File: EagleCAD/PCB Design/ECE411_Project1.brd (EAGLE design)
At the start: 160 x 100 mm, 38 parts, among them J1 0473460001_USBMICRO, U1 ATS160SM-1, U2 MIC29310-5.0WU, U3 NCP5501DT50RKG, U4 DCJACK_2.1MM_PTH

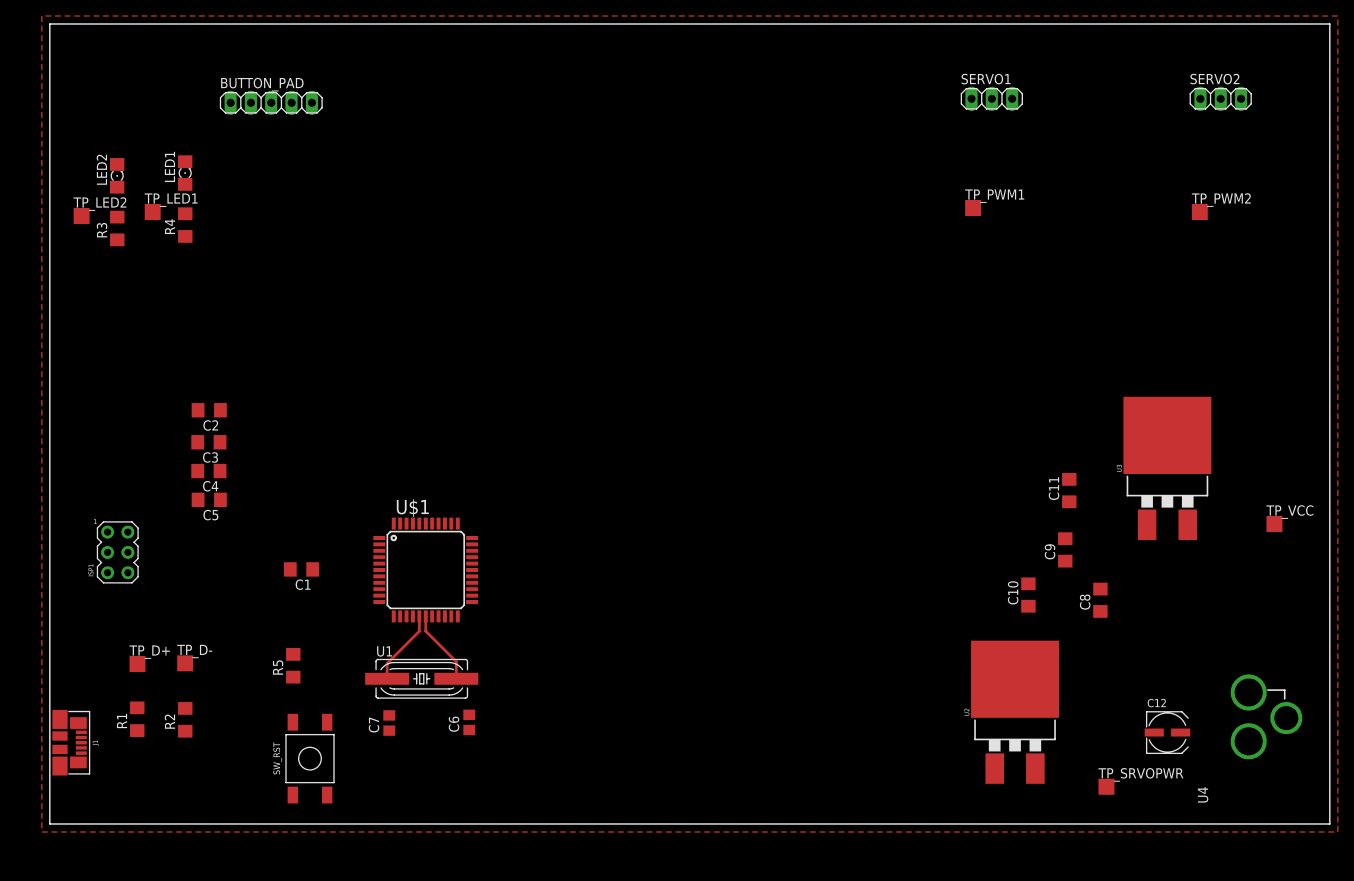
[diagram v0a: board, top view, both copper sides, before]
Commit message: in-progress updates: Connected Vbuses in schematic, organized the new layout design
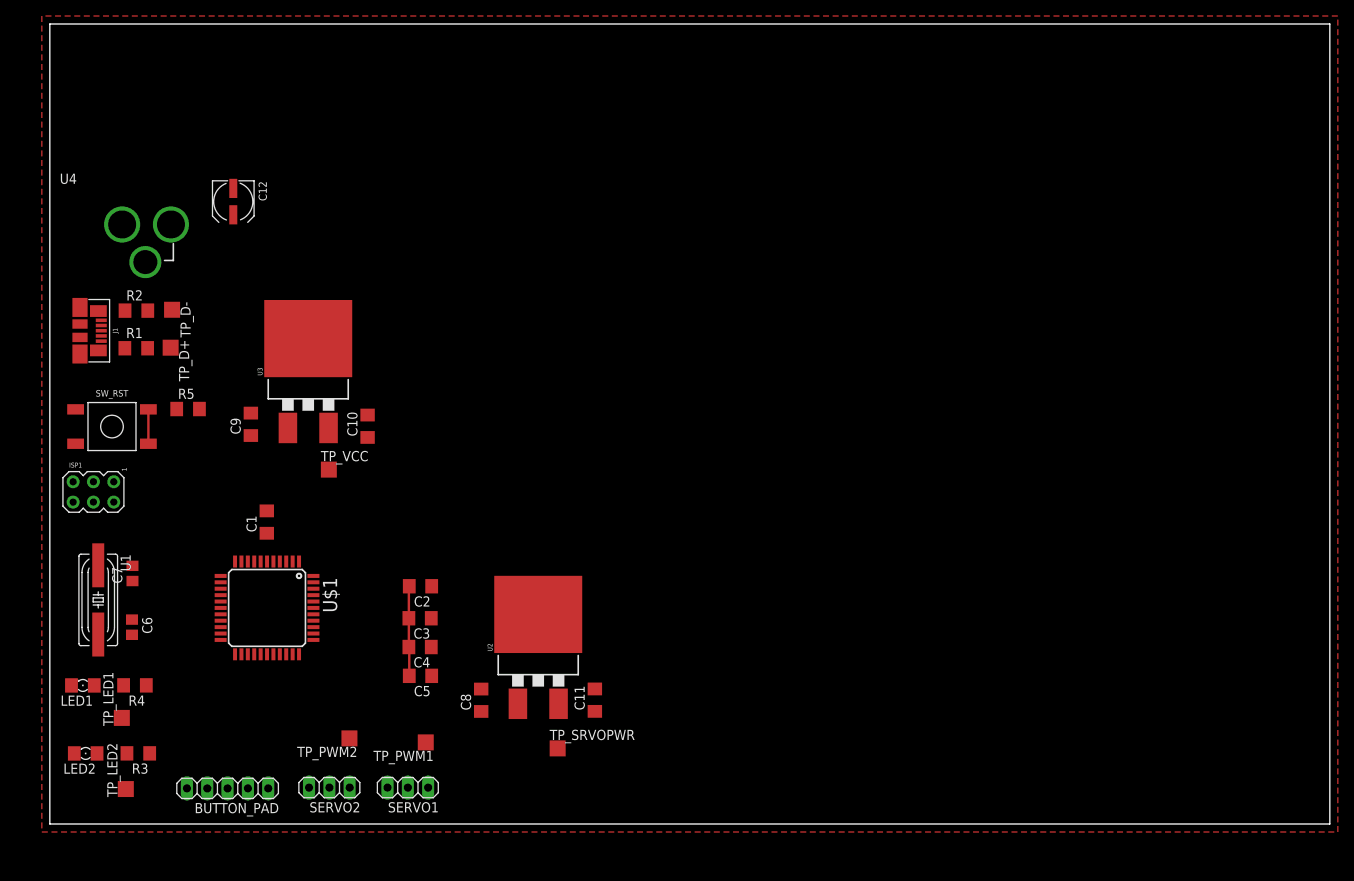
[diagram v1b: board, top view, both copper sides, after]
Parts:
- moved U4 165.3 mm to (1.24, 74.9), turned to 270 degrees
- moved SERVO2 140.8 mm to (34.9, 4.55), turned to 180 degrees
- moved C12 134.3 mm to (22.9, 77.8), turned to 270 degrees
- moved TP_PWM2 125.0 mm to (37.5, 10.7), turned to 180 degrees
- moved TP_VCC 118.4 mm to (34.9, 44.3)
- moved SERVO1 112.9 mm to (44.8, 4.55), turned to 180 degrees
- moved U3 108.1 mm to (32.3, 56.5)
- moved C9 103.0 mm to (25.1, 50.0)
- moved TP_PWM1 95.6 mm to (47.0, 10.2), turned to 180 degrees
- moved BUTTON_PAD 85.9 mm to (22.2, 4.45), turned to 180 degrees
- moved C10 85.3 mm to (39.7, 49.7)
- moved C8 78.4 mm to (53.9, 15.5)
- moved LED2 72.3 mm to (4.48, 8.82), turned to 180 degrees
- moved TP_LED2 71.8 mm to (9.50, 4.37), turned to 90 degrees
- moved TP_SRVOPWR 68.8 mm to (63.5, 9.45)
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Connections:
- removed net VBUS: J1.1
- new net N$1: J1.1, U$1.7
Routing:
- net VCC: track 0.00 -> 11.2 mm
- net XTAL2: track 9.47 -> 0.00 mm
- net XTAL1: track 9.38 -> 0.00 mm
- net /RST: track 0.00 -> 4.30 mm

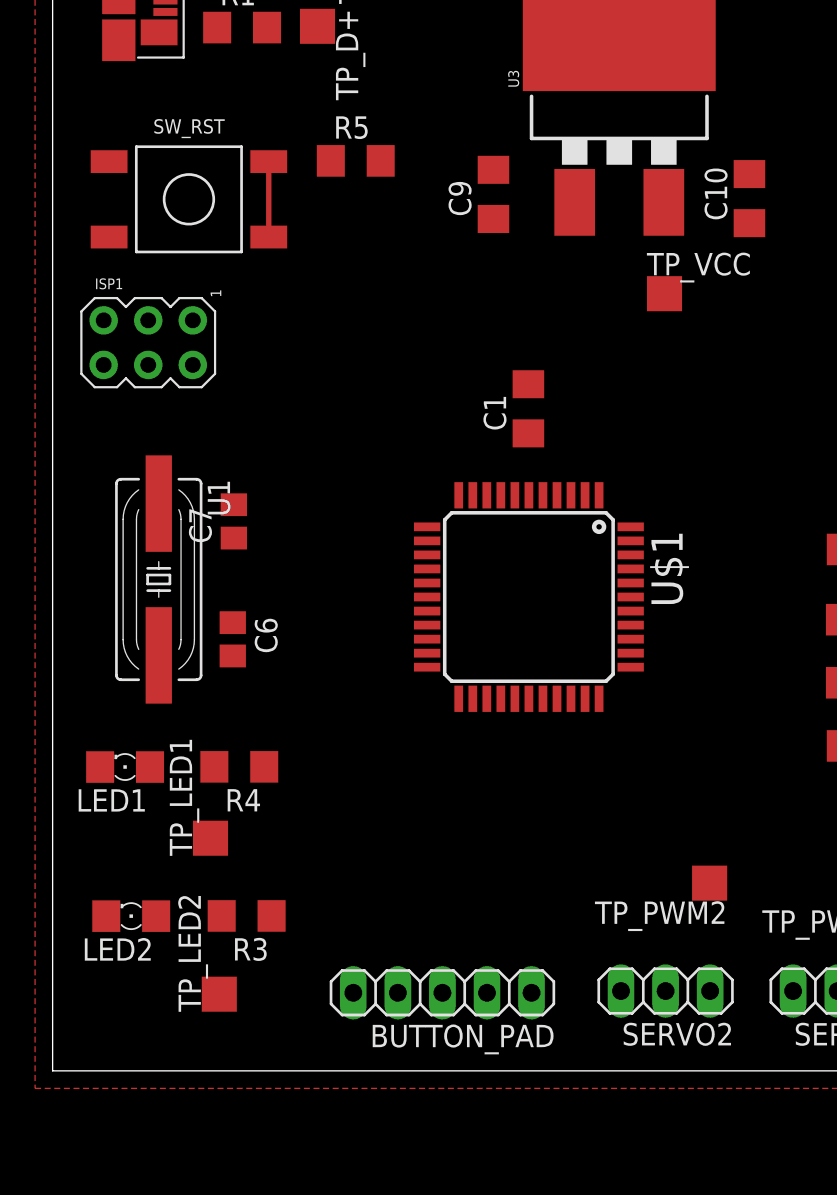
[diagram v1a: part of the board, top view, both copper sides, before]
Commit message: In-progress updates: Connected UVCC to power and added a capacitor for it
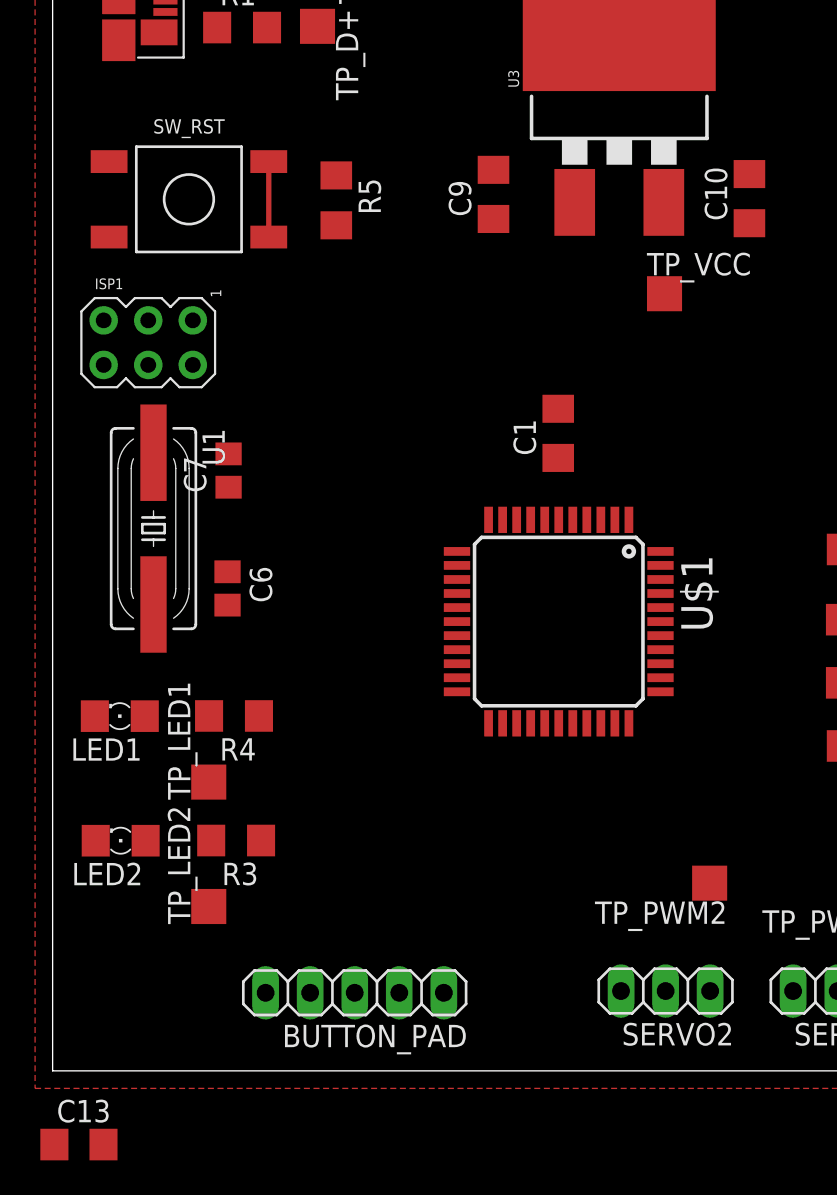
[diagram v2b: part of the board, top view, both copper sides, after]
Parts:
- added C13: 0.1u, rcl:C1206
- moved TP_LED2 5.04 mm to (8.90, 9.37)
- moved BUTTON_PAD 5.00 mm to (17.2, 4.45)
- moved R3 4.34 mm to (10.5, 13.1)
- moved LED2 4.34 mm to (3.88, 13.1)
- moved TP_LED1 3.20 mm to (8.90, 16.5)
- moved R4 2.92 mm to (10.3, 20.2)
- moved C7 2.92 mm to (10.0, 34.2)
- moved C6 2.92 mm to (9.97, 27.5)
- moved LED1 2.92 mm to (3.83, 20.2)
- moved U1 2.92 mm to (5.75, 30.9)
- moved R5 2.51 mm to (16.2, 49.6), turned to 270 degrees
- moved U$1 2.20 mm to (28.9, 25.6)
- moved C1 2.20 mm to (28.8, 36.3)
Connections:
- net GND: now also C13.1
- net VCC: now also C13.2, U$1.2

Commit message: In-Progress Updates: Still fitting out the layout board file
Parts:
- moved U4 73.5 mm to (67.5, 43.0), turned to 90 degrees
- moved C13 48.9 mm to (46.5, 15.0), turned to 180 degrees
- moved C12 44.1 mm to (45.8, 40.1), turned to 90 degrees
- moved C3 1.33 mm to (46.6, 27.0)
- moved C2 1.32 mm to (46.5, 31.0)
- moved C4 0.95 mm to (46.6, 23.0)
- moved ISP1 0.58 mm to (5.95, 41.8)
- moved C5 0.54 mm to (46.5, 19.0)
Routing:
- net VCC: track 11.2 -> 16.9 mm
- net UCAP: track 0.00 -> 3.54 mm

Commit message: In progress - almost finished layout
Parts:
- moved J1 68.4 mm to (36.8, 1.77), turned to 90 degrees
- moved U4 68.1 mm to (1.54, 60.0), turned to 270 degrees
- moved R2 60.1 mm to (34.3, 8.82), turned to 90 degrees
- moved R1 58.0 mm to (39.0, 8.80), turned to 90 degrees
- moved TP_D- 54.4 mm to (34.2, 13.3), turned to 0 degrees
- moved TP_D+ 52.2 mm to (39.0, 13.1), turned to 0 degrees
- moved U2 44.6 mm to (42.0, 62.4)
- moved C12 43.7 mm to (13.5, 69.5), turned to 0 degrees
- moved C11 41.4 mm to (46.0, 50.5), turned to 0 degrees
- moved TP_SRVOPWR 40.3 mm to (47.5, 46.5)
- moved C8 36.6 mm to (39.7, 49.2), turned to 270 degrees
- moved C5 32.8 mm to (15.0, 28.0), turned to 0 degrees
- moved SERVO1 32.0 mm to (45.0, 36.5), turned to 270 degrees
- moved TP_PWM1 29.5 mm to (40.5, 39.0), turned to 270 degrees
- moved C4 26.0 mm to (22.0, 14.4), turned to 90 degrees
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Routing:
- net UNREG_PWR: track 0.00 -> 70.6 mm
- net VCC: track 16.9 -> 65.9 mm, vias 0 -> 1
- net SERVO_PWR: track 0.00 -> 44.1 mm
- net D-MCU: track 0.00 -> 32.5 mm, vias 0 -> 2
- net N$13: track 0.00 -> 30.7 mm
- net D+MCU: track 0.00 -> 30.4 mm, vias 0 -> 2
- net N$11: track 0.00 -> 28.3 mm
- net N$7: track 0.00 -> 28.1 mm
- net N$6: track 0.00 -> 23.3 mm
- net N$12: track 0.00 -> 17.6 mm, vias 0 -> 1
- net XTAL2: track 0.00 -> 17.3 mm
- net N$8: track 0.00 -> 16.9 mm
- net XTAL1: track 0.00 -> 15.8 mm
- net /RST: track 4.30 -> 17.3 mm
- net PWM1: track 0.00 -> 4.52 mm
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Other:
- board size 160 x 100 mm -> 50 x 80 mm

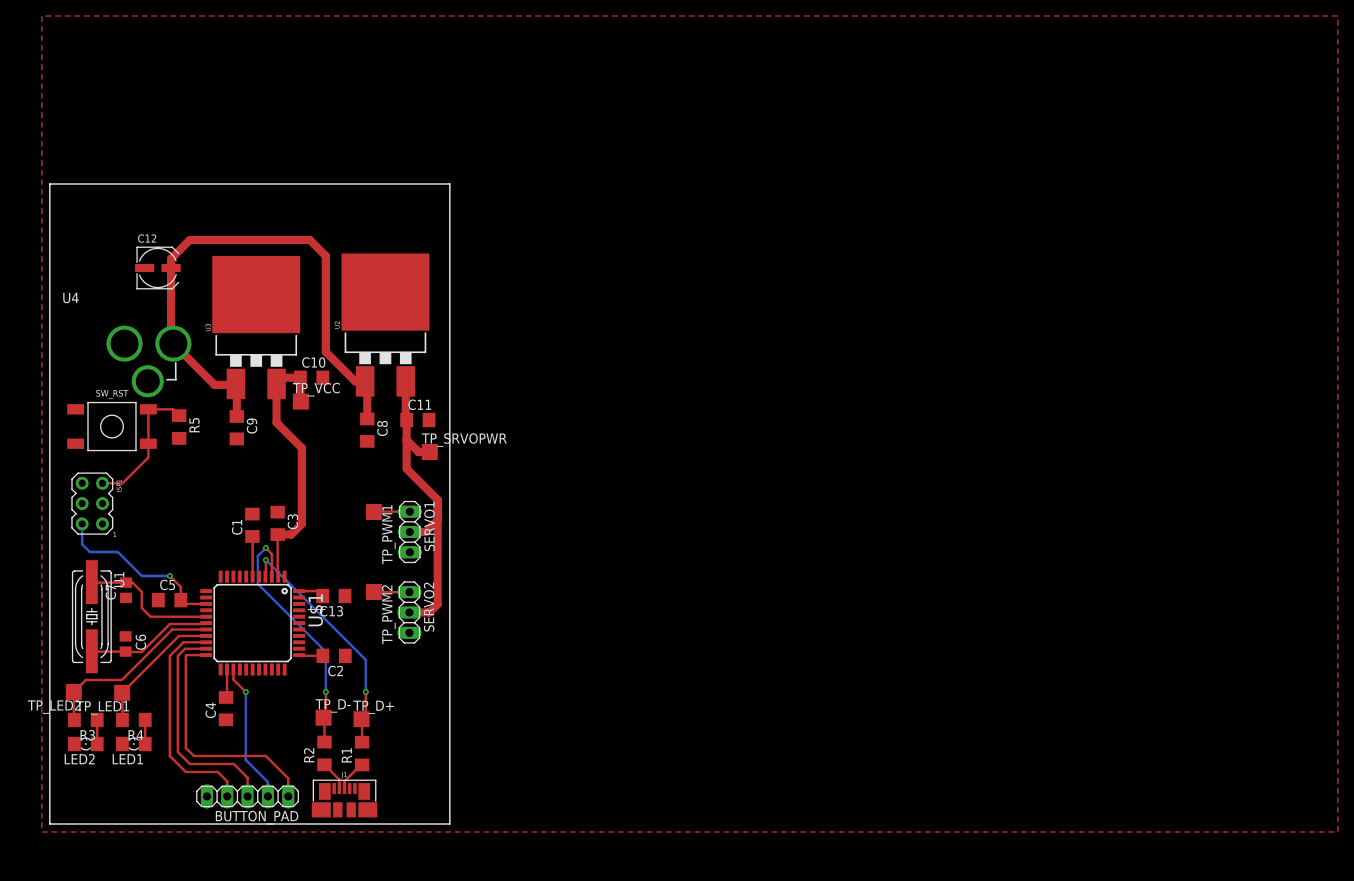
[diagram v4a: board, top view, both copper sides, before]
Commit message: updated BOM, completed Layout. Still need to add team number and project description to schematic
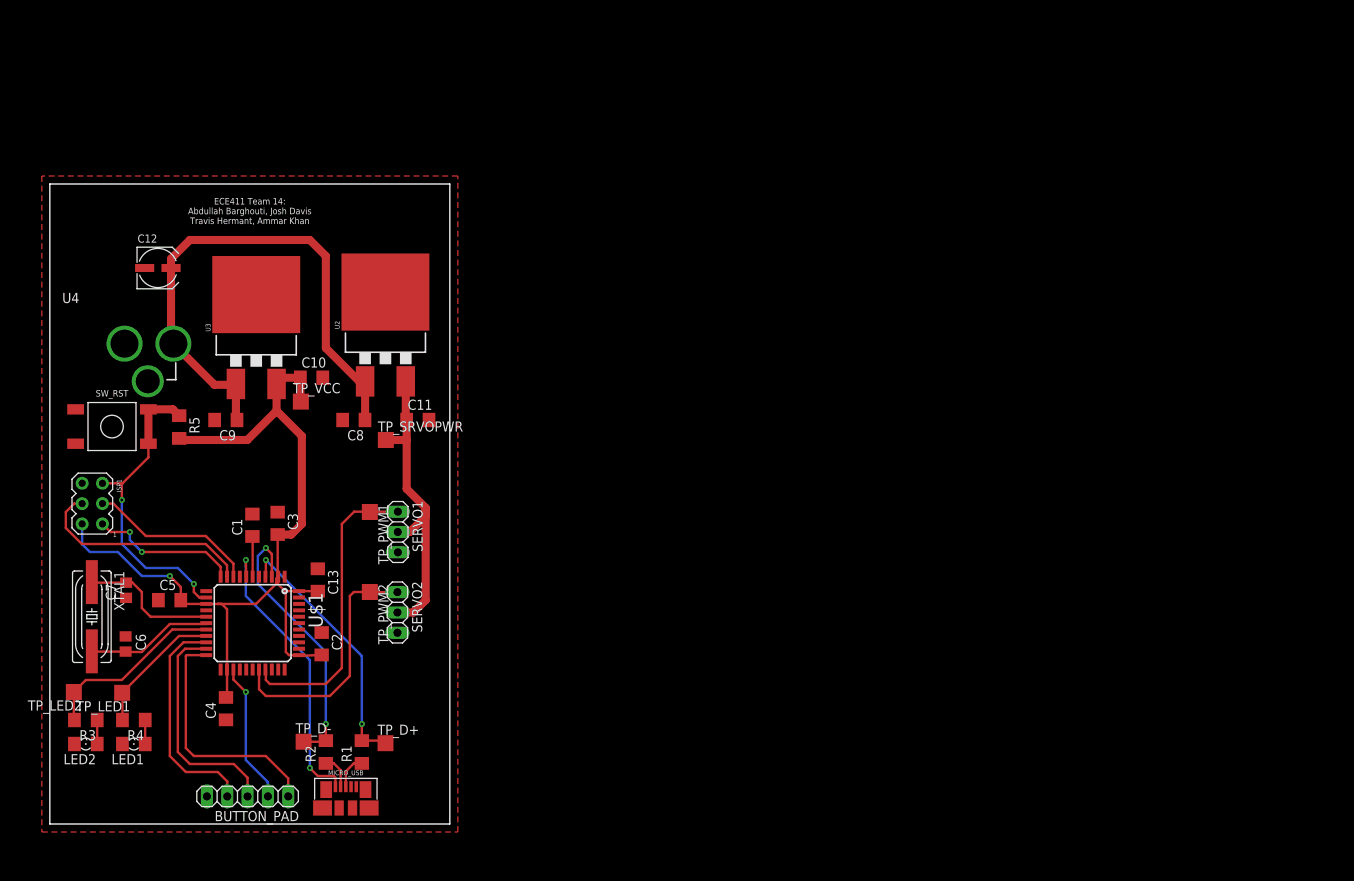
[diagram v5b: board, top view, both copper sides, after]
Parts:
- removed J1: 0473460001_USBMICRO, USB_Micro_and_AVRISP:MOLEX_USBMICRO
- added MICRO_USB: 0473460001_USBMICRO, USB_Micro_and_AVRISP:MOLEX_USBMICRO
- XTAL1: value ATS160SM-1 -> 16MHz
- moved TP_SRVOPWR 5.70 mm to (42.0, 48.0)
- moved TP_D+ 4.24 mm to (42.0, 10.1)
- moved TP_D- 3.91 mm to (31.7, 10.3)
- moved C13 2.83 mm to (33.5, 30.5), turned to 270 degrees
- moved C2 2.16 mm to (34.0, 22.5), turned to 270 degrees
- moved C8 2.11 mm to (38.0, 50.5), turned to 180 degrees
- moved C9 1.67 mm to (22.0, 50.5), turned to 180 degrees
- moved SERVO1 1.50 mm to (43.5, 36.5)
- moved SERVO2 1.50 mm to (43.5, 26.4)
- moved TP_PWM1 0.50 mm to (40.0, 39.0)
- moved TP_PWM2 0.50 mm to (40.0, 29.0)
- moved R2 0.25 mm to (34.5, 9.00)
- moved R1 0.20 mm to (39.0, 9.00)
- renumbered U1 to XTAL1
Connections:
- removed net GNDBREAK: U4.GNDBREAK
- removed net N$1: J1.1, U$1.7
- new net VBUS: MICRO_USB.1, U$1.7
- net D+USB: now also MICRO_USB.3; no longer J1.3
- net D-USB: now also MICRO_USB.2; no longer J1.2
- net GND: now also MICRO_USB.5, MICRO_USB.G1, MICRO_USB.G2, MICRO_USB.G3, MICRO_USB.G4, MICRO_USB.G5, MICRO_USB.G6, U4.GNDBREAK; no longer J1.5, J1.G1, J1.G2, J1.G3, J1.G4, J1.G5, J1.G6
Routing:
- net VCC: track 65.9 -> 111.8 mm
- net VBUS: track 0.00 -> 36.2 mm, vias 0 -> 2
- net PWM1: track 4.52 -> 37.7 mm
- net N$17: track 0.00 -> 28.0 mm
- net PWM2: track 4.46 -> 31.4 mm
- net /RST: track 17.3 -> 38.8 mm, vias 0 -> 2
- net N$18: track 0.00 -> 21.1 mm
- net N$16: track 0.00 -> 18.8 mm, vias 0 -> 2
- net SERVO_PWR: track 44.1 -> 40.5 mm
- net D+MCU: track 30.4 -> 33.2 mm
- net D-MCU: track 32.5 -> 34.8 mm
- net UNREG_PWR: track 70.6 -> 69.6 mm
- net D-USB: track 3.74 -> 4.27 mm
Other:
- board text added: "ECE411 Team 14: Abdullah Barghouti, Josh Davis Travis Hermant, Ammar Khan"
